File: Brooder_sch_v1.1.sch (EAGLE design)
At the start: 38 parts, among them J1 DCJ0202, J2 1X2-3.5MM, J3 DCJ0202, J4 1X2-3.5MM, T1 2N2222, U1 328P

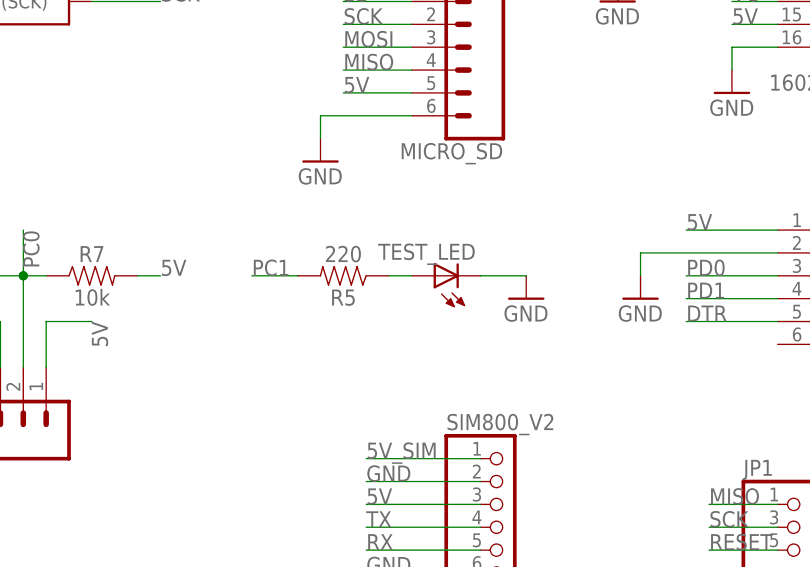
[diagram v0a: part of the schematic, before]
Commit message: Removes test led fro  schematic
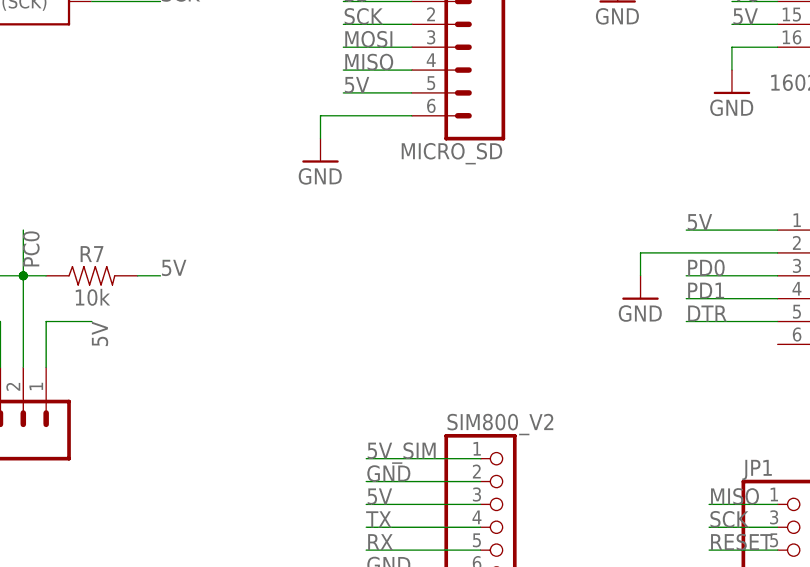
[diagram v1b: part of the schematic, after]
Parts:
- removed R5: 220, SparkFun-Resistors:10MOHM-HORIZ-1/4W-5%
- removed TEST_LED: (no value), adafruit:LED5MM
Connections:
- removed net N$1: R5.1, TEST_LED.A
- net GND: no longer TEST_LED.C
- net PC1: no longer R5.2
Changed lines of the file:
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@@
 <part name="GND18" library="supply1" library_urn="urn:adsk.eagle:library:371" deviceset="GND" device=""/>
 <part name="J2" library="adafruit" deviceset="1X2" device="-3.5MM"/>
-<part name="R5" library="SparkFun-Resistors" deviceset="10MOHM" device="-HORIZ-1/4W-5%" value="220"/>
-<part name="TEST_LED" library="adafruit" deviceset="LED" device="5MM"/>
-<part name="GND16" library="supply1" library_urn="urn:adsk.eagle:library:371" deviceset="GND" device=""/>
 <part name="DS3231" library="SparkFun-Connectors" deviceset="CONN_06" device="NO_SILK_FEMALE_PTH"/>
 <part name="GND25" library="supply1" library_urn="urn:adsk.eagle:library:371" deviceset="GND" device=""/>
@@
 </instance>
 <instance part="J2" gate="G$1" x="-55.88" y="121.92" rot="R90"/>
-<instance part="R5" gate="G$1" x="104.14" y="15.24" smashed="yes" rot="R180">
-<attribute name="NAME" x="104.14" y="13.716" size="1.778" layer="95" font="vector" rot="R180" align="bottom-center"/>
-<attribute name="VALUE" x="104.14" y="16.764" size="1.778" layer="96" font="vector" rot="R180" align="top-center"/>
-</instance>
-<instance part="TEST_LED" gate="G$1" x="114.3" y="15.24" smashed="yes" rot="R90">
-<attribute name="NAME" x="118.872" y="18.796" size="1.778" layer="95" rot="R180"/>
-<attribute name="VALUE" x="118.872" y="20.955" size="1.778" layer="96" rot="R180"/>
-</instance>
-<instance part="GND16" gate="1" x="124.46" y="12.7" smashed="yes">
-<attribute name="VALUE" x="121.92" y="10.16" size="1.778" layer="96"/>
-</instance>
 <instance part="DS3231" gate="G$1" x="114.3" y="71.12" smashed="yes" rot="R180">
 <attribute name="VALUE" x="119.38" y="81.026" size="1.778" layer="96" font="vector" rot="R180"/>
@@
 <wire x1="137.16" y1="17.78" x2="137.16" y2="15.24" width="0.1524" layer="91"/>
 <pinref part="GND18" gate="1" pin="GND"/>
-</segment>
-<segment>
-<pinref part="TEST_LED" gate="G$1" pin="C"/>
-<pinref part="GND16" gate="1" pin="GND"/>
-<wire x1="119.38" y1="15.24" x2="124.46" y2="15.24" width="0.1524" layer="91"/>
 </segment>
 <segment>
@@
 </segment>
 </net>
-<net name="N$1" class="0">
-<segment>
-<pinref part="R5" gate="G$1" pin="1"/>
-<pinref part="TEST_LED" gate="G$1" pin="A"/>
-<wire x1="109.22" y1="15.24" x2="111.76" y2="15.24" width="0.1524" layer="91"/>
-</segment>
-</net>
 <net name="PC1" class="0">
 <segment>
@@
 </segment>
 <segment>
-<pinref part="R5" gate="G$1" pin="2"/>
-<wire x1="99.06" y1="15.24" x2="93.98" y2="15.24" width="0.1524" layer="91"/>
-<label x="93.98" y="15.24" size="1.778" layer="95"/>
-</segment>
-<segment>

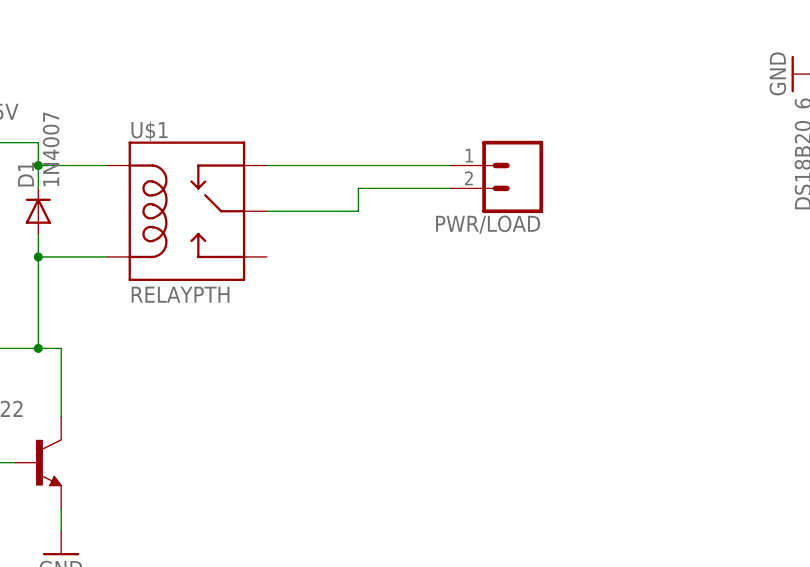
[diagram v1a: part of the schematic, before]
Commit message: Adds extra terminal block to the relay
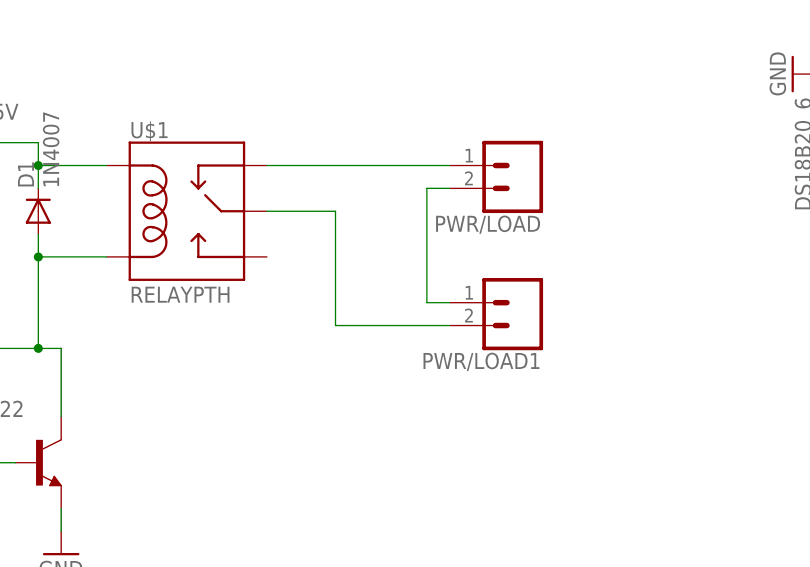
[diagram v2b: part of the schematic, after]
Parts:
- added PWR/LOAD1: (no value), SparkFun-Connectors:CONN_025MM
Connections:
- removed net N$14: PWR/LOAD.2, U$1.SWCOMMON
- new net N$1: PWR/LOAD1.2, U$1.SWCOMMON
- new net N$3: PWR/LOAD.2, PWR/LOAD1.1
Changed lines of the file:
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@@
 <part name="LED2" library="adafruit" deviceset="LED" device="5MM"/>
 <part name="GND22" library="supply1" library_urn="urn:adsk.eagle:library:371" deviceset="GND" device=""/>
+<part name="PWR/LOAD1" library="SparkFun-Connectors" deviceset="CONN_02" device="5MM"/>
 </parts>
 <sheets>
@@
 <instance part="GND22" gate="1" x="-43.18" y="-43.18" smashed="yes">
 <attribute name="VALUE" x="-45.72" y="-45.72" size="1.778" layer="96"/>
+</instance>
+<instance part="PWR/LOAD1" gate="G$1" x="7.62" y="-15.24" smashed="yes" rot="R180">
+<attribute name="VALUE" x="10.16" y="-10.414" size="1.778" layer="96" font="vector" rot="R180"/>
+<attribute name="NAME" x="10.16" y="-20.828" size="1.778" layer="95" font="vector" rot="R180"/>
 </instance>
 </instances>
@@
 </segment>
 </net>
-<net name="N$14" class="0">
-<segment>
+<net name="N$1" class="0">
+<segment>
+<pinref part="PWR/LOAD1" gate="G$1" pin="2"/>
+<wire x1="0" y1="-17.78" x2="-12.7" y2="-17.78" width="0.1524" layer="91"/>
+<wire x1="-12.7" y1="-17.78" x2="-12.7" y2="-5.08" width="0.1524" layer="91"/>
 <pinref part="U$1" gate="G$1" pin="SWCOMMON"/>
+<wire x1="-12.7" y1="-5.08" x2="-20.32" y2="-5.08" width="0.1524" layer="91"/>
+</segment>
+</net>
+<net name="N$3" class="0">
+<segment>
 <pinref part="PWR/LOAD" gate="G$1" pin="2"/>
-<wire x1="0" y1="-2.54" x2="-10.16" y2="-2.54" width="0.1524" layer="91"/>
-<wire x1="-10.16" y1="-2.54" x2="-10.16" y2="-5.08" width="0.1524" layer="91"/>
-<wire x1="-10.16" y1="-5.08" x2="-20.32" y2="-5.08" width="0.1524" layer="91"/>
-</segment>
-</net>
+<wire x1="0" y1="-2.54" x2="-2.54" y2="-2.54" width="0.1524" layer="91"/>
+<wire x1="-2.54" y1="-2.54" x2="-2.54" y2="-15.24" width="0.1524" layer="91"/>
+<pinref part="PWR/LOAD1" gate="G$1" pin="1"/>
+<wire x1="-2.54" y1="-15.24" x2="0" y2="-15.24" width="0.1524" layer="91"/>
+</segment>
+</net>

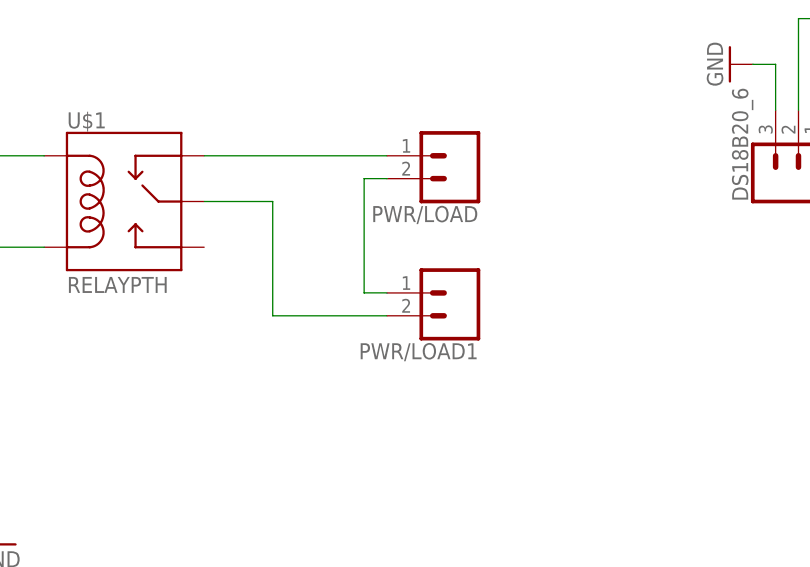
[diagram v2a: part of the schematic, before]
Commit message: Replaces ds3231 header pins with ds3231 symbol
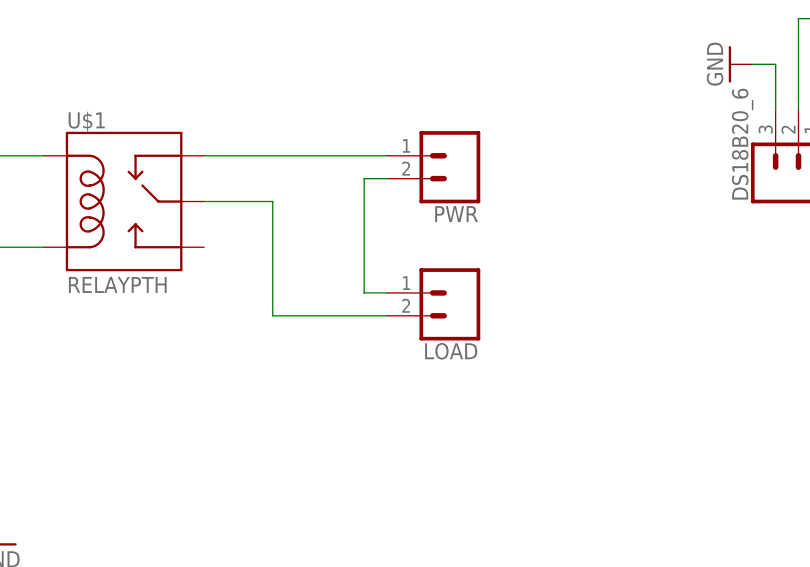
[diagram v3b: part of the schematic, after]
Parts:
- renumbered PWR/LOAD to PWR, PWR/LOAD1 to LOAD
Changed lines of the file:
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@@
 <part name="D1" library="adafruit" deviceset="1N4004" device="" value="1N4007"/>
 <part name="T1" library="adafruit" deviceset="2N2222" device=""/>
-<part name="PWR/LOAD" library="SparkFun-Connectors" deviceset="CONN_02" device="5MM"/>
+<part name="PWR" library="SparkFun-Connectors" deviceset="CONN_02" device="5MM"/>
 <part name="R4" library="SparkFun-Resistors" deviceset="10MOHM" device="-HORIZ-1/4W-5%" value="220"/>
 <part name="R6" library="SparkFun-Resistors" deviceset="10MOHM" device="-HORIZ-1/4W-5%" value="1k"/>
 <part name="LED2" library="adafruit" deviceset="LED" device="5MM"/>
 <part name="GND22" library="supply1" library_urn="urn:adsk.eagle:library:371" deviceset="GND" device=""/>
-<part name="PWR/LOAD1" library="SparkFun-Connectors" deviceset="CONN_02" device="5MM"/>
+<part name="LOAD" library="SparkFun-Connectors" deviceset="CONN_02" device="5MM"/>
 </parts>
 <sheets>
@@
 <attribute name="VALUE" x="-55.88" y="-27.94" size="1.778" layer="96"/>
 </instance>
-<instance part="PWR/LOAD" gate="G$1" x="7.62" y="0" smashed="yes" rot="R180">
+<instance part="PWR" gate="G$1" x="7.62" y="0" smashed="yes" rot="R180">
 <attribute name="VALUE" x="10.16" y="4.826" size="1.778" layer="96" font="vector" rot="R180"/>
 <attribute name="NAME" x="10.16" y="-5.588" size="1.778" layer="95" font="vector" rot="R180"/>
@@
 <attribute name="VALUE" x="-45.72" y="-45.72" size="1.778" layer="96"/>
 </instance>
-<instance part="PWR/LOAD1" gate="G$1" x="7.62" y="-15.24" smashed="yes" rot="R180">
+<instance part="LOAD" gate="G$1" x="7.62" y="-15.24" smashed="yes" rot="R180">
 <attribute name="VALUE" x="10.16" y="-10.414" size="1.778" layer="96" font="vector" rot="R180"/>
 <attribute name="NAME" x="10.16" y="-20.828" size="1.778" layer="95" font="vector" rot="R180"/>
@@
 <net name="N$13" class="0">
 <segment>
-<pinref part="PWR/LOAD" gate="G$1" pin="1"/>
+<pinref part="PWR" gate="G$1" pin="1"/>
 <wire x1="-20.32" y1="0" x2="0" y2="0" width="0.1524" layer="91"/>
 <pinref part="U$1" gate="G$1" pin="SWCLOSE"/>
@@
 <net name="N$1" class="0">
 <segment>
-<pinref part="PWR/LOAD1" gate="G$1" pin="2"/>
+<pinref part="LOAD" gate="G$1" pin="2"/>
 <wire x1="0" y1="-17.78" x2="-12.7" y2="-17.78" width="0.1524" layer="91"/>
 <wire x1="-12.7" y1="-17.78" x2="-12.7" y2="-5.08" width="0.1524" layer="91"/>
@@
 <net name="N$3" class="0">
 <segment>
-<pinref part="PWR/LOAD" gate="G$1" pin="2"/>
+<pinref part="PWR" gate="G$1" pin="2"/>
 <wire x1="0" y1="-2.54" x2="-2.54" y2="-2.54" width="0.1524" layer="91"/>
 <wire x1="-2.54" y1="-2.54" x2="-2.54" y2="-15.24" width="0.1524" layer="91"/>
-<pinref part="PWR/LOAD1" gate="G$1" pin="1"/>
+<pinref part="LOAD" gate="G$1" pin="1"/>
 <wire x1="-2.54" y1="-15.24" x2="0" y2="-15.24" width="0.1524" layer="91"/>
 </segment>
